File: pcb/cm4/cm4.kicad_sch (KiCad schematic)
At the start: 1 part, among them J101 Conn_02x10_Row_Letter_First

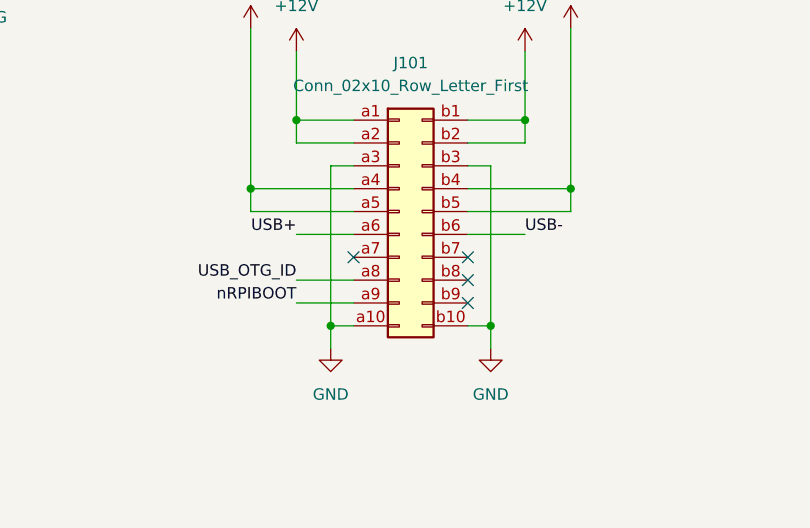
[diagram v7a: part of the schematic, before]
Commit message: fix pin assignment
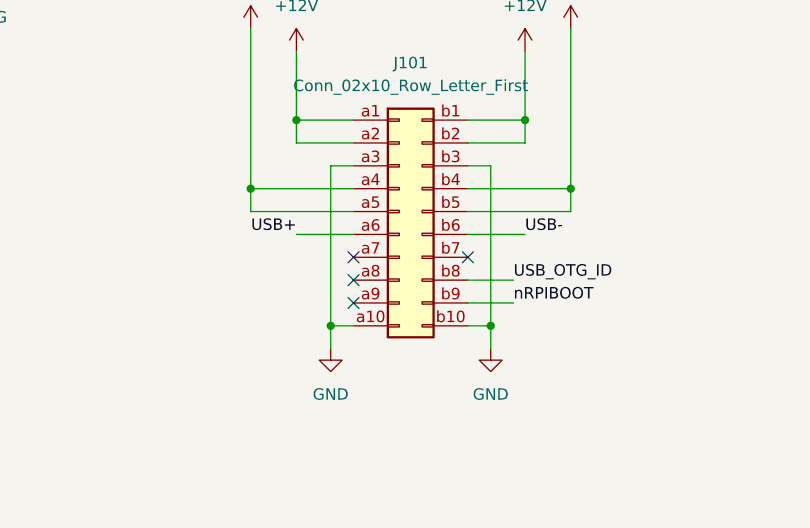
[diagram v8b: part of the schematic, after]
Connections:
- net USB_OTG_ID: now also J101.b8 (Pin_b8); no longer J101.a8 (Pin_a8)
- net nRPIBOOT: now also J101.b9 (Pin_b9); no longer J101.a9 (Pin_a9)
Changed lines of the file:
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@@
 	)
 	(no_connect
-		(at 88.9 118.11)
-	)
-	(no_connect
-		(at 88.9 115.57)
+		(at 76.2 115.57)
 	)
 	(no_connect
 		(at 76.2 113.03)
 	)
+	(no_connect
+		(at 76.2 118.11)
+	)
 	(wire
 		(pts
@@
 	(wire
 		(pts
-			(xy 69.85 118.11) (xy 76.2 118.11)
-		)
-		(stroke
-			(width 0)
-			(type default)
-		)
-	)
-	(wire
-		(pts
 			(xy 195.58 81.28) (xy 213.36 81.28)
 		)
@@
 	(wire
 		(pts
-			(xy 69.85 115.57) (xy 76.2 115.57)
-		)
-		(stroke
-			(width 0)
-			(type default)
-		)
-	)
-	(wire
-		(pts
 			(xy 69.85 100.33) (xy 69.85 97.79)
 		)
@@
 	(wire
 		(pts
+			(xy 88.9 118.11) (xy 93.98 118.11)
+		)
+		(stroke
+			(width 0)
+			(type default)
+		)
+	)
+	(wire
+		(pts
 			(xy 195.58 123.19) (xy 213.36 123.19)
 		)
@@
 	(wire
 		(pts
+			(xy 88.9 115.57) (xy 93.98 115.57)
+		)
+		(stroke
+			(width 0)
+			(type default)
+		)
+	)
+	(wire
+		(pts
 			(xy 33.02 71.12) (xy 33.02 69.85)
 		)
@@
 	)
 	(label "USB_OTG_ID"
-		(at 69.85 115.57 180)
-		(effects
-			(font
-				(size 1.27 1.27)
-			)
-			(justify right bottom)
+		(at 93.98 115.57 0)
+		(effects
+			(font
+				(size 1.27 1.27)
+			)
+			(justify left bottom)
 		)
 	)
@@
 	)
 	(label "nRPIBOOT"
-		(at 69.85 118.11 180)
-		(effects
-			(font
-				(size 1.27 1.27)
-			)
-			(justify right bottom)
-		)
-	)
+		(at 93.98 118.11 0)
+		(effects
+			(font
+				(size 1.27 1.27)
+			)
+			(justify left bottom)
+		)
+	)
